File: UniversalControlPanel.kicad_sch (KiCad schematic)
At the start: 15 parts

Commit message: components
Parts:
- removed U?: MAX485E, symbol Interface_UART:MAX485E
- added U?: MAX14783ExS, Package_SO:SOIC-8_3.9x4.9mm_P1.27mm, symbol Interface_UART:MAX14783ExS
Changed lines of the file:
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@@
     (pin "1")
   )
-  (symbol (lib_id "Interface_UART:MAX485E") (at 76.2 163.83 0) (unit 1)
-    (in_bom yes) (on_board yes) (fields_autoplaced)
-    (property "Reference" "U?" (id 0) (at 78.2194 148.59 0)
-      (effects (font (size 1.27 1.27)) (justify left))
-    )
-    (property "Value" "MAX485E" (id 1) (at 78.2194 151.13 0)
-      (effects (font (size 1.27 1.27)) (justify left))
-    )
-    (property "Footprint" "" (id 2) (at 76.2 181.61 0)
-      (effects (font (size 1.27 1.27)) hide)
-    )
-    (property "Datasheet" "https://datasheets.maximintegrated.com/en/ds/MAX1487E-MAX491E.pdf" (id 3) (at 76.2 162.56 0)
+  (symbol (lib_id "power:+5V") (at 54.61 27.94 0) (unit 1)
+    (in_bom yes) (on_board yes) (fields_autoplaced)
+    (property "Reference" "#PWR?" (id 0) (at 54.61 31.75 0)
+      (effects (font (size 1.27 1.27)) hide)
+    )
+    (property "Value" "+5V" (id 1) (at 54.61 22.86 0))
+    (property "Footprint" "" (id 2) (at 54.61 27.94 0)
+      (effects (font (size 1.27 1.27)) hide)
+    )
+    (property "Datasheet" "" (id 3) (at 54.61 27.94 0)
+      (effects (font (size 1.27 1.27)) hide)
+    )
+    (pin "1")
+  )
+  (symbol (lib_id "Connector:Conn_01x04_Male") (at 227.33 41.91 0) (unit 1)
+    (in_bom yes) (on_board yes) (fields_autoplaced)
+    (property "Reference" "J?" (id 0) (at 227.965 34.29 0))
+    (property "Value" "Conn_01x04_Male" (id 1) (at 227.965 36.83 0))
+    (property "Footprint" "" (id 2) (at 227.33 41.91 0)
+      (effects (font (size 1.27 1.27)) hide)
+    )
+    (property "Datasheet" "~" (id 3) (at 227.33 41.91 0)
+      (effects (font (size 1.27 1.27)) hide)
+    )
+    (pin "1")
+    (pin "2")
+    (pin "3")
+    (pin "4")
+  )
+  (symbol (lib_id "Connector:Conn_01x04_Male") (at 226.06 25.4 0) (unit 1)
+    (in_bom yes) (on_board yes) (fields_autoplaced)
+    (property "Reference" "J?" (id 0) (at 226.695 17.78 0))
+    (property "Value" "Conn_01x04_Male" (id 1) (at 226.695 20.32 0))
+    (property "Footprint" "" (id 2) (at 226.06 25.4 0)
+      (effects (font (size 1.27 1.27)) hide)
+    )
+    (property "Datasheet" "~" (id 3) (at 226.06 25.4 0)
+      (effects (font (size 1.27 1.27)) hide)
+    )
+    (pin "1")
+    (pin "2")
+    (pin "3")
+    (pin "4")
+  )
+  (symbol (lib_id "Device:C") (at 54.61 31.75 0) (unit 1)
+    (in_bom yes) (on_board yes) (fields_autoplaced)
+    (property "Reference" "C?" (id 0) (at 58.42 30.4799 0)
+      (effects (font (size 1.27 1.27)) (justify left))
+    )
+    (property "Value" "10u" (id 1) (at 58.42 33.0199 0)
+      (effects (font (size 1.27 1.27)) (justify left))
+    )
+    (property "Footprint" "" (id 2) (at 55.5752 35.56 0)
+      (effects (font (size 1.27 1.27)) hide)
+    )
+    (property "Datasheet" "~" (id 3) (at 54.61 31.75 0)
+      (effects (font (size 1.27 1.27)) hide)
+    )
+    (pin "1")
+    (pin "2")
+  )
+  (symbol (lib_id "power:+3.3V") (at 40.64 66.04 0) (unit 1)
+    (in_bom yes) (on_board yes) (fields_autoplaced)
+    (property "Reference" "#PWR?" (id 0) (at 40.64 69.85 0)
+      (effects (font (size 1.27 1.27)) hide)
+    )
+    (property "Value" "+3.3V" (id 1) (at 40.64 60.96 0))
+    (property "Footprint" "" (id 2) (at 40.64 66.04 0)
+      (effects (font (size 1.27 1.27)) hide)
+    )
+    (property "Datasheet" "" (id 3) (at 40.64 66.04 0)
+      (effects (font (size 1.27 1.27)) hide)
+    )
+    (pin "1")
+  )
+  (symbol (lib_id "Interface_UART:MAX14783ExS") (at 43.18 166.37 0) (unit 1)
+    (in_bom yes) (on_board yes) (fields_autoplaced)
+    (property "Reference" "U?" (id 0) (at 45.1994 151.13 0)
+      (effects (font (size 1.27 1.27)) (justify left))
+    )
+    (property "Value" "MAX14783ExS" (id 1) (at 45.1994 153.67 0)
+      (effects (font (size 1.27 1.27)) (justify left))
+    )
+    (property "Footprint" "Package_SO:SOIC-8_3.9x4.9mm_P1.27mm" (id 2) (at 43.18 189.23 0)
+      (effects (font (size 1.27 1.27)) hide)
+    )
+    (property "Datasheet" "https://datasheets.maximintegrated.com/en/ds/MAX14783E.pdf" (id 3) (at 43.18 165.1 0)
       (effects (font (size 1.27 1.27)) hide)
     )
@@
     (pin "8")
   )
-  (symbol (lib_id "power:+5V") (at 54.61 27.94 0) (unit 1)
-    (in_bom yes) (on_board yes) (fields_autoplaced)
-    (property "Reference" "#PWR?" (id 0) (at 54.61 31.75 0)
-      (effects (font (size 1.27 1.27)) hide)
-    )
-    (property "Value" "+5V" (id 1) (at 54.61 22.86 0))
-    (property "Footprint" "" (id 2) (at 54.61 27.94 0)
-      (effects (font (size 1.27 1.27)) hide)
-    )
-    (property "Datasheet" "" (id 3) (at 54.61 27.94 0)
-      (effects (font (size 1.27 1.27)) hide)
-    )
-    (pin "1")
-  )
-  (symbol (lib_id "Connector:Conn_01x04_Male") (at 227.33 41.91 0) (unit 1)
-    (in_bom yes) (on_board yes) (fields_autoplaced)
-    (property "Reference" "J?" (id 0) (at 227.965 34.29 0))
-    (property "Value" "Conn_01x04_Male" (id 1) (at 227.965 36.83 0))
-    (property "Footprint" "" (id 2) (at 227.33 41.91 0)
-      (effects (font (size 1.27 1.27)) hide)
-    )
-    (property "Datasheet" "~" (id 3) (at 227.33 41.91 0)
-      (effects (font (size 1.27 1.27)) hide)
-    )
-    (pin "1")
-    (pin "2")
-    (pin "3")
-    (pin "4")
-  )
-  (symbol (lib_id "Connector:Conn_01x04_Male") (at 226.06 25.4 0) (unit 1)
-    (in_bom yes) (on_board yes) (fields_autoplaced)
-    (property "Reference" "J?" (id 0) (at 226.695 17.78 0))
-    (property "Value" "Conn_01x04_Male" (id 1) (at 226.695 20.32 0))
-    (property "Footprint" "" (id 2) (at 226.06 25.4 0)
-      (effects (font (size 1.27 1.27)) hide)
-    )
-    (property "Datasheet" "~" (id 3) (at 226.06 25.4 0)
-      (effects (font (size 1.27 1.27)) hide)
-    )
-    (pin "1")
-    (pin "2")
-    (pin "3")
-    (pin "4")
-  )
-  (symbol (lib_id "Device:C") (at 54.61 31.75 0) (unit 1)
-    (in_bom yes) (on_board yes) (fields_autoplaced)
-    (property "Reference" "C?" (id 0) (at 58.42 30.4799 0)
-      (effects (font (size 1.27 1.27)) (justify left))
-    )
-    (property "Value" "10u" (id 1) (at 58.42 33.0199 0)
-      (effects (font (size 1.27 1.27)) (justify left))
-    )
-    (property "Footprint" "" (id 2) (at 55.5752 35.56 0)
-      (effects (font (size 1.27 1.27)) hide)
-    )
-    (property "Datasheet" "~" (id 3) (at 54.61 31.75 0)
-      (effects (font (size 1.27 1.27)) hide)
-    )
-    (pin "1")
-    (pin "2")
-  )
-  (symbol (lib_id "power:+3.3V") (at 40.64 66.04 0) (unit 1)
-    (in_bom yes) (on_board yes) (fields_autoplaced)
-    (property "Reference" "#PWR?" (id 0) (at 40.64 69.85 0)
-      (effects (font (size 1.27 1.27)) hide)
-    )
-    (property "Value" "+3.3V" (id 1) (at 40.64 60.96 0))
-    (property "Footprint" "" (id 2) (at 40.64 66.04 0)
-      (effects (font (size 1.27 1.27)) hide)
-    )
-    (property "Datasheet" "" (id 3) (at 40.64 66.04 0)
-      (effects (font (size 1.27 1.27)) hide)
-    )
-    (pin "1")
-  )
   (symbol (lib_id "power:GND") (at 21.59 85.09 0) (unit 1)
     (in_bom yes) (on_board yes) (fields_autoplaced)
@@
       (reference "U?") (unit 1) (value "ESP32-S2-WROVER-I") (footprint "RF_Module:ESP32-S2-WROVER")
     )
-    (path "/85b6ba73-120f-43b7-a126-cdbfe6ee119f"
-      (reference "U?") (unit 1) (value "MAX485E") (footprint "")
+    (path "/b4501435-1b74-4814-ac8d-457d48a8c57b"
+      (reference "U?") (unit 1) (value "MAX14783ExS") (footprint "Package_SO:SOIC-8_3.9x4.9mm_P1.27mm")
     )
     (path "/b7ac5cea-ed28-4028-87d0-45e58c709cf1"

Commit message: wip
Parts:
- removed J? (x2): Conn_01x04_Male, symbol Connector:Conn_01x04_Male
- removed U?: MCP2515-xST, Package_SO:TSSOP-20_4.4x6.5mm_P0.65mm, symbol Interface_CAN_LIN:MCP2515-xST
- added D1: B5819W SL, Diode_SMD:D_SOD-123, symbol Device:D_Schottky
- added D2, D3, D4, D5: SM4007, Diode_SMD:D_MELF, symbol Diode:SM4007
- added J1: USB_B_Micro, symbol Connector:USB_B_Micro
- added J2: Conn_ARM_JTAG_SWD_10, symbol Connector:Conn_ARM_JTAG_SWD_10
- added J4: Conn_02x03_Odd_Even, symbol Connector_Generic:Conn_02x03_Odd_Even
- added Q1, Q2, Q3, Q4: 2N7002, Package_TO_SOT_SMD:SOT-23, symbol Transistor_FET:2N7002
- added R10, R13, R15, R8: 100k, symbol Device:R
- added R11, R12, R14, R4, R5, R6, R7, R9: R, symbol Device:R
- added R2, R3: 10k, symbol Device:R
- added U3: USBLC6-2SC6, Package_TO_SOT_SMD:SOT-23-6, symbol Power_Protection:USBLC6-2SC6
- added U5, U7: LMV321, symbol Amplifier_Operational:LMV321
- J3: renamed from J?; footprint (none) -> Connector_FFC-FPC:TE_4-1734839-0_1x40-1MP_P0.5mm_Horizontal
- gave numbers to parts that had none: 11
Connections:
- net +3V3: now also J3.12 (Pin_12), J3.3 (Pin_3), U2.8 (VCC), J2.1 (VTref), J4.2 (Pin_2), R2.1, R3.1
- net +5V: now also J3.33 (Pin_33), D1.1 (K), U3.5 (VBUS)
- net CHIP_PU: now also J2.10 (~{RESET}), J4.1 (Pin_1)
- net GND: now also J3.1 (Pin_1), J3.14 (Pin_14), J3.15 (Pin_15), J3.16 (Pin_16), J3.17 (Pin_17), J3.18 (Pin_18), J3.19 (Pin_19), J3.20 (Pin_20), J3.21 (Pin_21), J3.22 (Pin_22), J3.23 (Pin_23), J3.24 (Pin_24), J3.25 (Pin_25), J3.26 (Pin_26), J3.27 (Pin_27), J3.28 (Pin_28), J3.29 (Pin_29), J3.30 (Pin_30), J3.40 (Pin_40), U2.5 (GND), J1.5 (GND), J1.6 (Shield), J2.3 (GND), J2.5 (GND), J2.9 (GNDDetect), J4.4 (Pin_4), Q1.2 (S), Q2.2 (S), Q3.2 (S), Q4.2 (S), R10.2, R13.2, R15.2, R4.1, R5.2, R6.1, R7.2, R8.2, R9.1, U3.2 (GND), U5.2 (V-), U7.2 (V-)
- net U0RXD: now also J4.5 (Pin_5)
- net U0TXD: now also J4.3 (Pin_3)
- net WR(D/C): now reaches J3.11 (Pin_11)
- net WR(D/C): now also U6.27 (IO33)
- net SDO: now reaches J3.13 (Pin_13)
- net SDO: now also U6.31 (IO37)
- net SDI(SDA): now reaches J3.2 (Pin_2)
- net SDI(SDA): now also U6.29 (IO35)
- net CTP-RST: now reaches J3.31 (Pin_31)
- net CTP-RST: now also U6.5 (IO02)
- net CTP-SDA: now reaches J3.32 (Pin_32)
- net CTP-SDA: now also U6.6 (IO03), R3.2
- net LEDK1: now reaches J3.34 (Pin_34)
- net LEDK1: now also R4.2
- net LEDK2: now reaches J3.35 (Pin_35)
- net LEDK2: now also R5.1
- net LEDK3: now reaches J3.36 (Pin_36)
- net LEDK3: now also R6.2
- net LEDK4: now reaches J3.37 (Pin_37)
- net LEDK4: now also R7.1
- net CTP-INT: now reaches J3.5 (Pin_5)
- net CTP-INT: now also U6.8 (IO05)
- net CTP-SCL: now reaches J3.6 (Pin_6)
- net CTP-SCL: now also U6.7 (IO04), R2.2
- net RESET: now reaches J3.7 (Pin_7)
- net RESET: now also U6.32 (IO38)
- net RS(SCL): now reaches J3.8 (Pin_8)
- net RS(SCL): now also U6.30 (IO36)
- net CS: now reaches J3.9 (Pin_9)
- net CS: now also U6.28 (IO34)
- net 485_DIR: now reaches U6.19 (IO16)
- net 485_DIR: now also U2.2 (~{RE}), U2.3 (DE)
- net U1TXD: now reaches U6.20 (IO17)
- net U1TXD: now also U2.4 (DI)
- net U1RXD: now reaches U6.21 (IO18)
- net U1RXD: now also U2.1 (RO)
- net USB_DN: now reaches U6.22 (USB_D-)
- net USB_DN: now also U3.1 (I/O1)
- net USB_DP: now reaches U6.23 (USB_D+)
- net USB_DP: now also U3.3 (I/O2)
- net IO0: now reaches U6.3 (IO00)
- net IO0: now also J4.6 (Pin_6)
- net TCK: now reaches U6.33 (IO39)
- net TCK: now also J2.4 (SWDCLK/TCK)
- net TDO: now reaches U6.34 (IO40)
- net TDO: now also J2.6 (SWO/TDO)
- net TDI: now reaches U6.35 (IO41)
- net TDI: now also J2.8 (NC/TDI)
- net TMS: now reaches U6.36 (IO42)
- net TMS: now also J2.2 (SWDIO/TMS)
- new net: Q4.1 (G), R15.1
- new net: D5.2 (A), Q4.3 (D)
- new net: J1.3 (D+), U3.4 (I/O2)
- new net: J1.2 (D-), U3.6 (I/O1)
- new net: R11.1, R9.2, U5.3 (-)
- new net: R11.2, R12.1, U5.4
- new net: R12.2, R14.1, U7.3 (-)
- new net: R14.2, U7.4
- new net: Q3.1 (G), R13.1
- new net: D4.2 (A), Q3.3 (D)
- new net: Q2.1 (G), R10.1
- new net: Q1.1 (G), R8.1
- new net: D2.2 (A), Q1.3 (D)
- new net: D3.2 (A), Q2.3 (D)
- new net VBUS: D1.2 (A), J1.1 (VBUS)
- no-connect marks 0 -> 4
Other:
- note added: "(FSPIHD)"
- note added: "1.3V drop.. not really great.."
- note added: "4DLCD-24320240 IL9341 FT6236V pin 1 is first from left from front"
- note added: "FSPICLK - CLK"
- note added: "FSPICS0 - CS"
- note added: "FSPID - MOSI"
- note added: "FSPIQ - MISO"
- note added: "IMO:1 = 4wSPI"
- note added: "Most pins from Feather ESP32-S2 (see pins_arduino.h)"
- note added: "Old:IO0"
- note added: "Old:IO13"
- note added: "Old:IO18"
- note added: "Old:IO2"
- note added: "Old:IO21"
- note added: "Old:IO22"
- note added: "Old:IO23"
- note added: "Old:IO35"
- note added: "Old:IO?"
- note added: "better: TLV4316"
- note added: "https://www.st.com/resource/en/application_note/dm00133498-signal-conditioning-differential-to-singleended-amplification-stmicroelectronics.pdf"
- note added: "perhaps a R (22E) and C to GND (22p)"
- note added: "programming, debugging"
- note added: "to display"
- note removed: "DNP"
- moved on the sheet: C2, C5, J3, R1, SW1, U6

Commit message: pcb first place
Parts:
- removed D2, D3, D4, D5: SM4007, Diode_SMD:D_MELF, symbol Diode:SM4007
- removed Q1, Q2, Q3, Q4: 2N7002, Package_TO_SOT_SMD:SOT-23, symbol Transistor_FET:2N7002
- removed R10, R13, R15, R8: 100k, symbol Device:R
- removed R11, R12, R14, R9: R, symbol Device:R
- removed U5, U7: LMV321, symbol Amplifier_Operational:LMV321
- C1: value C -> 10u; footprint (none) -> Capacitor_SMD:C_1206_3216Metric; LCSC (none) -> C13585
- C2: footprint (none) -> Capacitor_SMD:C_0402_1005Metric
- C3, C5: footprint (none) -> Capacitor_SMD:C_1206_3216Metric; LCSC (none) -> C13585
- C4: footprint (none) -> Capacitor_SMD:C_0402_1005Metric; LCSC (none) -> C1525
- J1: footprint (none) -> Connector_USB:USB_Mini-B_Tensility_54-00023_Vertical
- J2: footprint (none) -> Connector_PinHeader_1.27mm:PinHeader_2x05_P1.27mm_Vertical
- J4: footprint (none) -> Connector_PinHeader_2.54mm:PinHeader_2x03_P2.54mm_Vertical
- R1, R2, R3, R4, R5, R6, R7: footprint (none) -> Resistor_SMD:R_0402_1005Metric
- U6: value ESP32-S2-WROVER-I -> ESP32-S2-WROOM-I; LSCS (none) -> C967026
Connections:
- net AIN_3.3V: now reaches U6.10 (IO07)
- net PD_OUT_1: now reaches U6.11 (IO08)
- net PD_OUT_2: now reaches U6.12 (IO09)
- net PD_OUT_3: now reaches U6.13 (IO10)
- net PD_OUT_4: now reaches U6.14 (IO11)
- net AIN_10V: now reaches U6.9 (IO06)
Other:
- added sheet InputOutput (untitled.kicad_sch)
- note added: "WROOM=no PSRAM"
- note removed: "better: TLV4316"
- moved on the sheet: R2, R3, U6

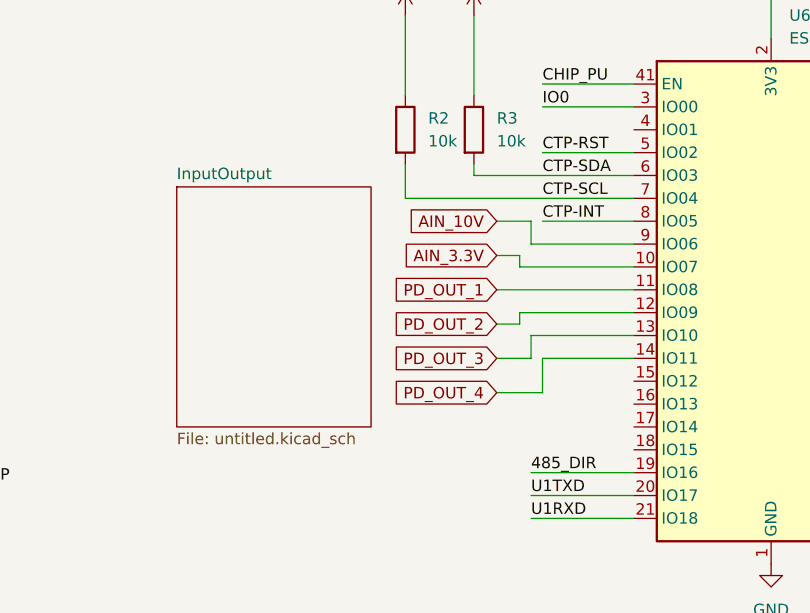
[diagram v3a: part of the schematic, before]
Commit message: moved input sch
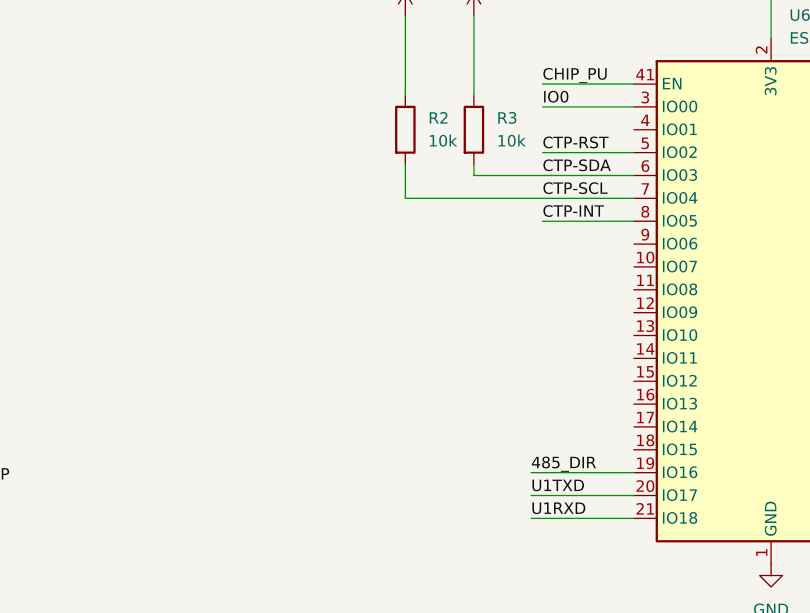
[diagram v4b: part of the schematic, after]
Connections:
- net AIN_10V: no longer names the net of U6.9 (IO06)
- net AIN_3.3V: no longer names the net of U6.10 (IO07)
- net PD_OUT_1: no longer names the net of U6.11 (IO08)
- net PD_OUT_2: no longer names the net of U6.12 (IO09)
- net PD_OUT_3: no longer names the net of U6.13 (IO10)
- net PD_OUT_4: no longer names the net of U6.14 (IO11)
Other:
- removed sheet InputOutput
